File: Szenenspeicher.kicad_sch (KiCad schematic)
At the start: 41 parts, among them J1 Conn_01x03_Pin, J2 Conn_01x03_Pin, J20 Conn_01x03_Pin, J30 Conn_01x02_Pin, J40 Conn_01x02_Pin, J50 Conn_01x02_Pin, J6 USB_A, J60 Conn_01x02_Pin, Q5 NPN, Q6 NPN, U1 ADM2483xRW, U10 SeeeduinoXIAO, U2 ADM2483xRW, U3 SGM809B-RXN3LG, U4 74LS26

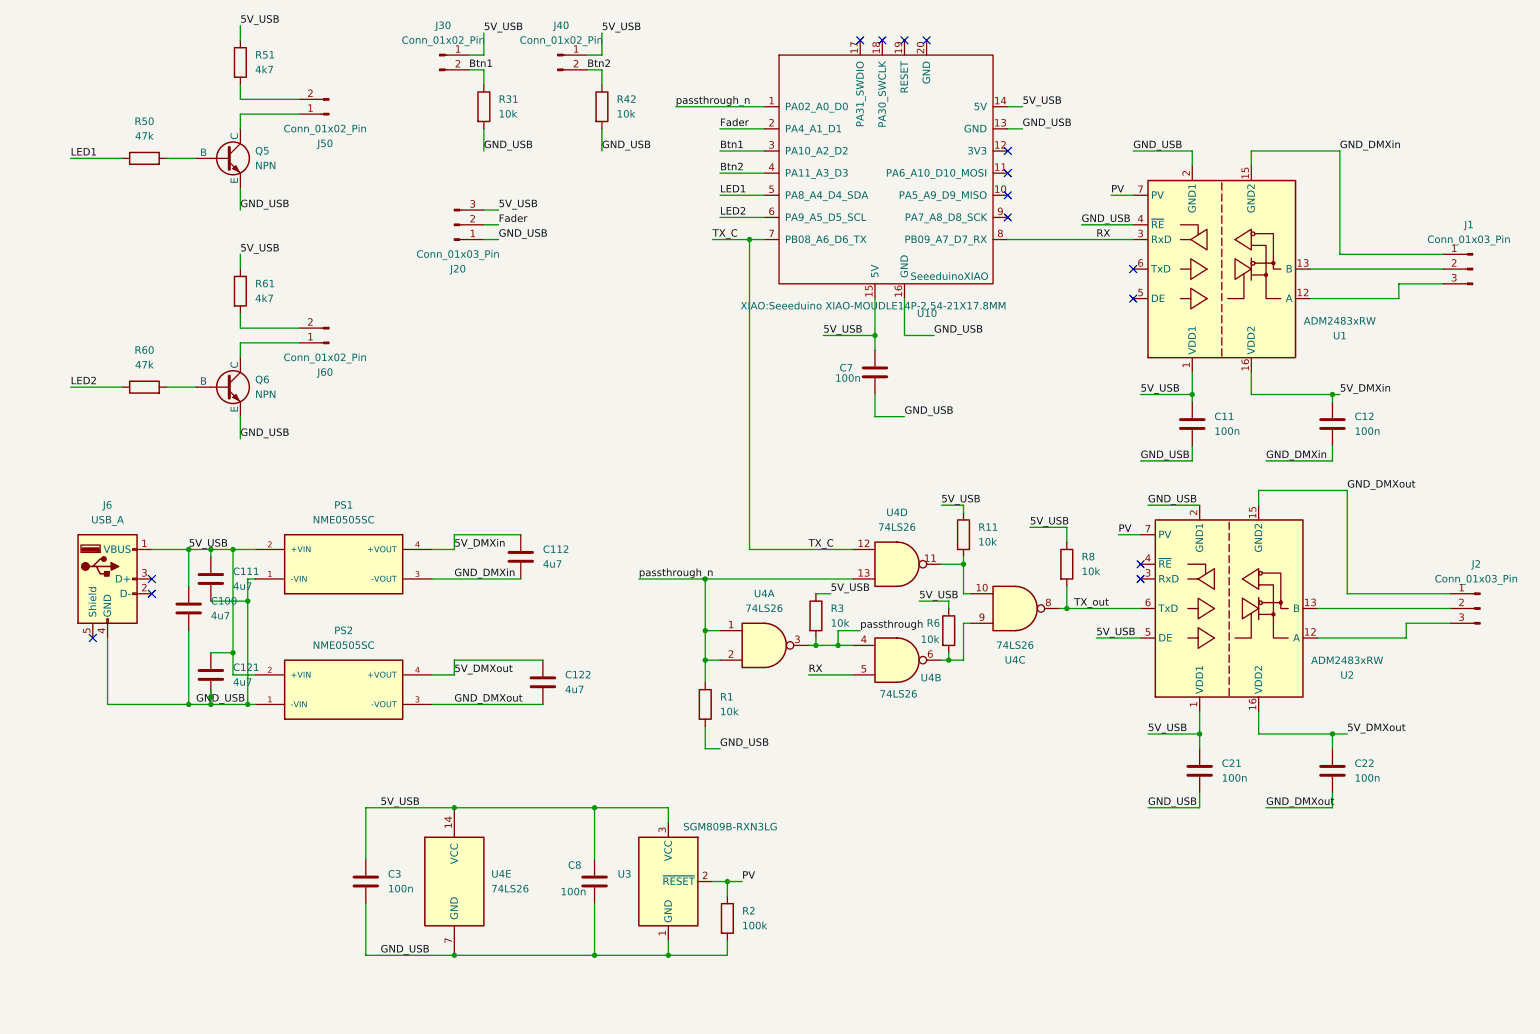
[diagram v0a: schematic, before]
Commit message: Signal supply changed to 3V3
* Signal supply changed to 3.3V in order to match ESP32-C6 specs
    - remark: using 3V3 regulator of XIAO board, as we need very little current. Leaving LED supply on 5V.
* base resistors of LED transistors adjusted to 10k
* collector resistors of LED supply adjusted to 330R
* layout modified in order to represent above changes
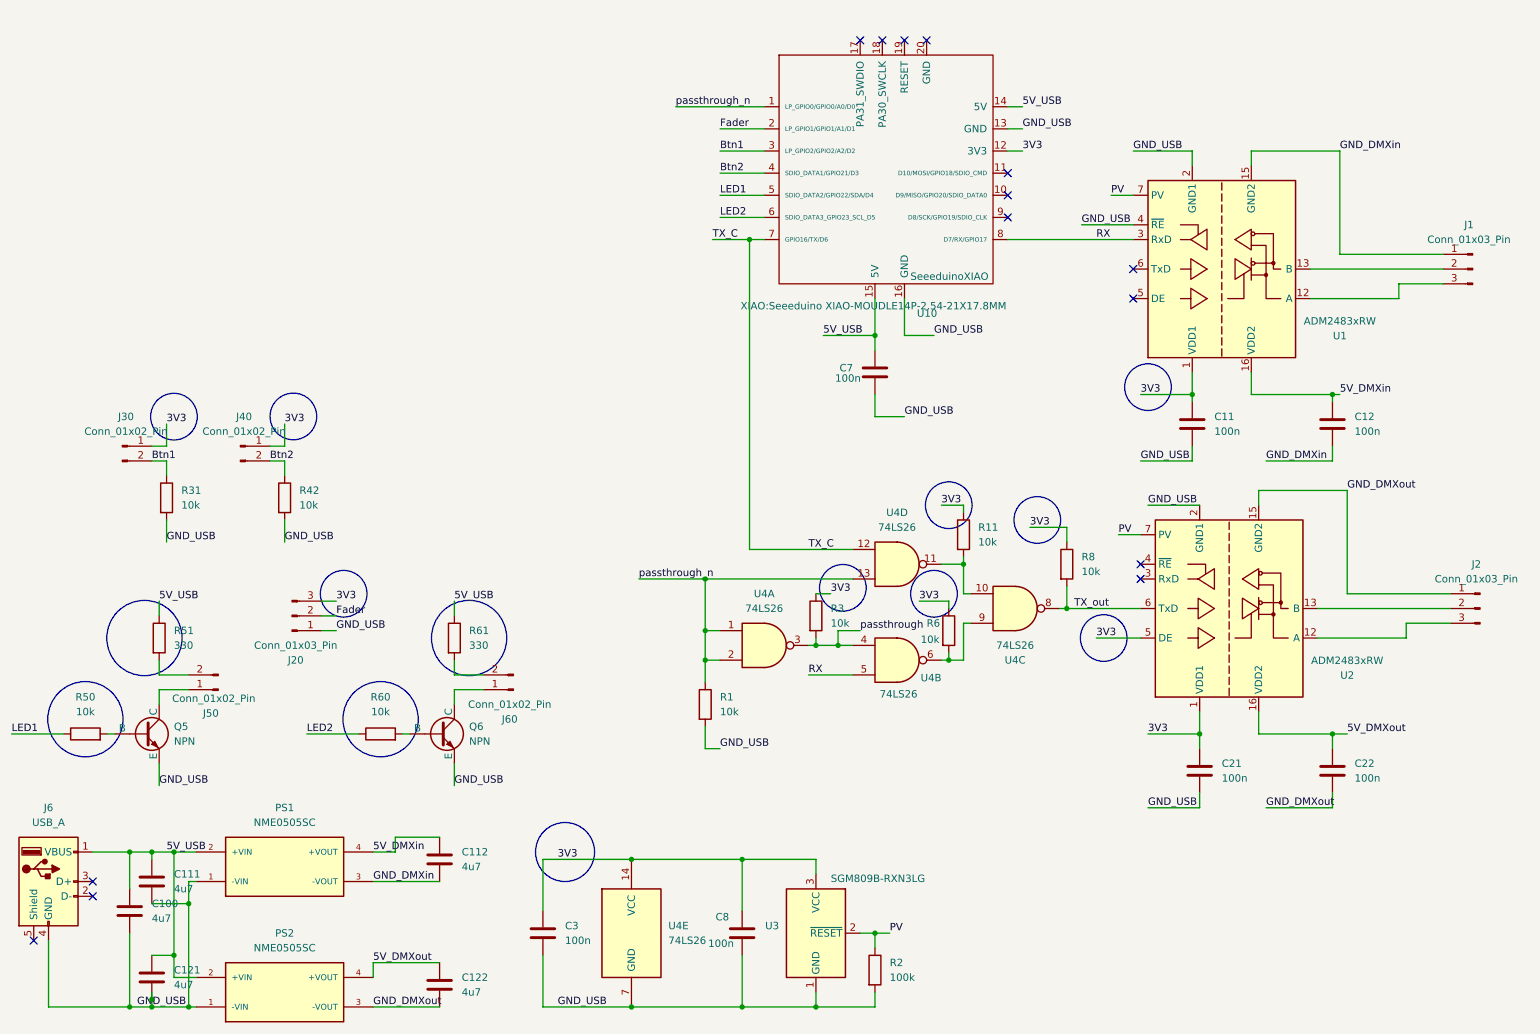
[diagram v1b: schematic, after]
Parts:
- R50, R60: value 47k -> 10k
- R51, R61: value 4k7 -> 330
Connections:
- net 5V_USB: no longer C11.1, C21.1, C3.1, C8.1, J20.3 (Pin_3), J30.1 (Pin_1), J40.1 (Pin_1), R11.1, R3.1, R6.1, R8.1, U1.1 (VDD1), U2.1 (VDD1), U2.5 (DE), U3.3 (VCC), U4.14 (VCC)
- net 3V3: now reaches U10.12 (3V3)
- net 3V3: now also C11.1, C21.1, C3.1, C8.1, J20.3 (Pin_3), J30.1 (Pin_1), J40.1 (Pin_1), R11.1, R3.1, R6.1, R8.1, U1.1 (VDD1), U2.1 (VDD1), U2.5 (DE), U3.3 (VCC), U4.14 (VCC)
- no-connect marks 15 -> 14
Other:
- moved on the sheet: C100, C111, C112, C121, C122, C3, C8, J20, J30, J40, J50, J6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
